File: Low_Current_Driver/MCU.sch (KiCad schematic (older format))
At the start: 13 parts, among them J9 Conn_01x02

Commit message: LCD amplifier update
- Updated OPA2277 amplifiers to OPA2210 that were actually populated on the boards.
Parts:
- A1: symbol Vernier_Vamp-2mA-rescue:Arduino_Nano_Every-MCU_Module-Vernier_Vamp-2mA-rescue -> MCU_Module:Arduino_Nano_Every
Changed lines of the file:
@@
 $EndComp
 $Comp
-L Vernier_Vamp-2mA-rescue:Arduino_Nano_Every-MCU_Module-Vernier_Vamp-2mA-rescue A1
+L MCU_Module:Arduino_Nano_Every A1
 U 1 1 5FA2A758
 P 5850 3800

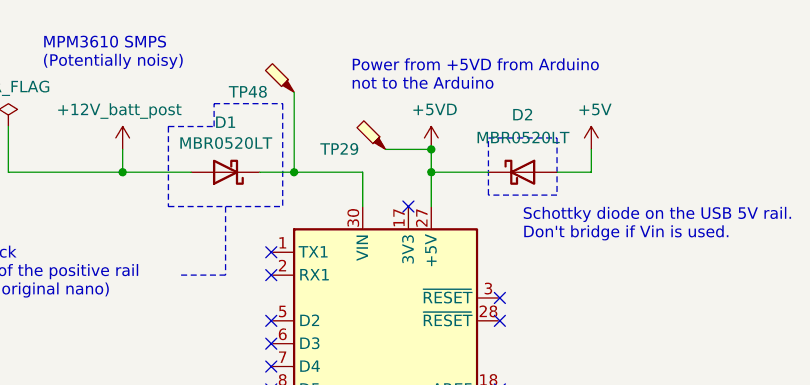
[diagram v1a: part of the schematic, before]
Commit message: Collection of minor fixes
- Added DNP to one of the power mux diodes
- Added missing power flag
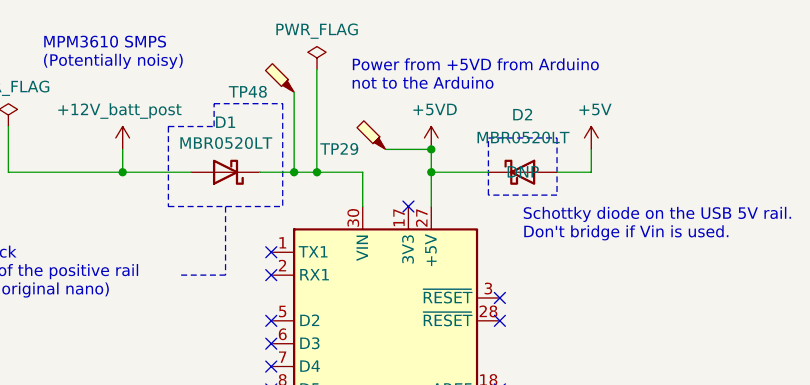
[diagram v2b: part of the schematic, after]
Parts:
- D2: DNP (none) -> DNP
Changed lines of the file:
@@
 Connection ~ 5450 2650
 Wire Wire Line
-	5450 2650 5750 2650
+	5450 2650 5550 2650
 Text HLabel 4700 4400 0    50   Output ~ 0
 SDO
@@
 F 2 "Diode_SMD:D_SOD-123" H 6450 2475 50  0001 C CNN
 F 3 "http://www.onsemi.com/pub_link/Collateral/MBR0520LT1-D.PDF" H 6450 2650 50  0001 C CNN
+F 4 "DNP" H 6450 2650 50  0000 C CNN "DNP"
 	1    6450 2650
 	1    0    0    -1
@@
 Text Notes 750  5800 0    50   ~ 0
 Trigger output for calibration
+$Comp
+L power:PWR_FLAG #FLG0108
+U 1 1 62A04722
+P 5550 2200
+F 0 "#FLG0108" H 5550 2275 50  0001 C CNN
+F 1 "PWR_FLAG" H 5550 2373 50  0000 C CNN
+F 2 "" H 5550 2200 50  0001 C CNN
+F 3 "~" H 5550 2200 50  0001 C CNN
+	1    5550 2200
+	1    0    0    -1
+$EndComp
+Wire Wire Line
+	5550 2200 5550 2650
+Connection ~ 5550 2650
+Wire Wire Line
+	5550 2650 5750 2650
 $EndSCHEMATC
